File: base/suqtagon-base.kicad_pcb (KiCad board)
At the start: 2 copper layers, 100 x 86.6 mm, 13 parts

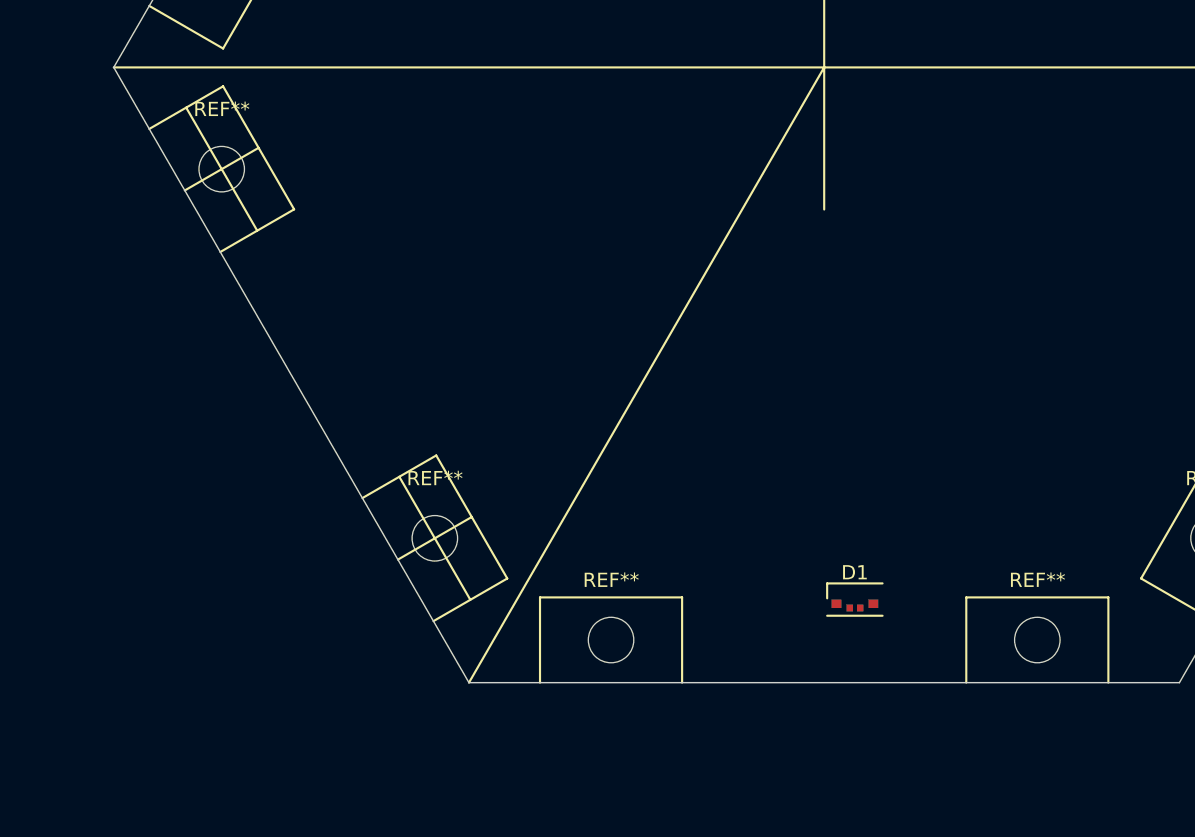
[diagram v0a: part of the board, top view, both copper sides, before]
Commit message: side single gerber
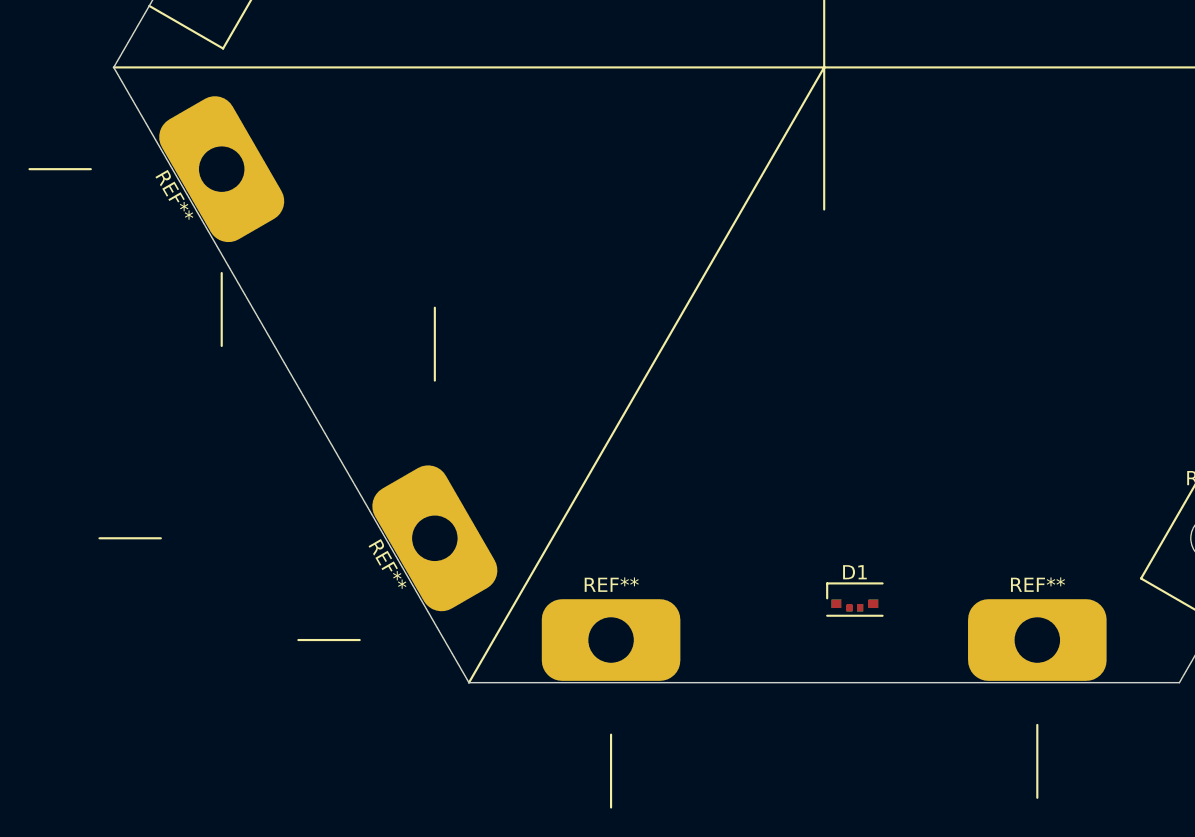
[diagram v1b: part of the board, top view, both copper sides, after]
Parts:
- removed the REF** at (57.6, 100.5)
- removed the REF** at (72.6, 126.4)
- removed the REF** at (85.0, 133.6)
- removed the REF** at (115.0, 133.6)
- added REF**: MountingHole_3.2mm_M3_ISO7380_Pad, MountingHoleConnector:MountingHole_3.2mm_M3_6mmx10mm_Pad, F.Cu at (115.0, 133.6)
- added REF**: MountingHole_3.2mm_M3_ISO7380_Pad, MountingHoleConnector:MountingHole_3.2mm_M3_6mmx10mm_Pad, F.Cu at (72.6, 126.4)
- added REF**: MountingHole_3.2mm_M3_ISO7380_Pad, MountingHoleConnector:MountingHole_3.2mm_M3_6mmx10mm_Pad, F.Cu at (57.6, 100.5)
- added REF**: MountingHole_3.2mm_M3_ISO7380_Pad, MountingHoleConnector:MountingHole_3.2mm_M3_6mmx10mm_Pad, F.Cu at (85.0, 133.6)

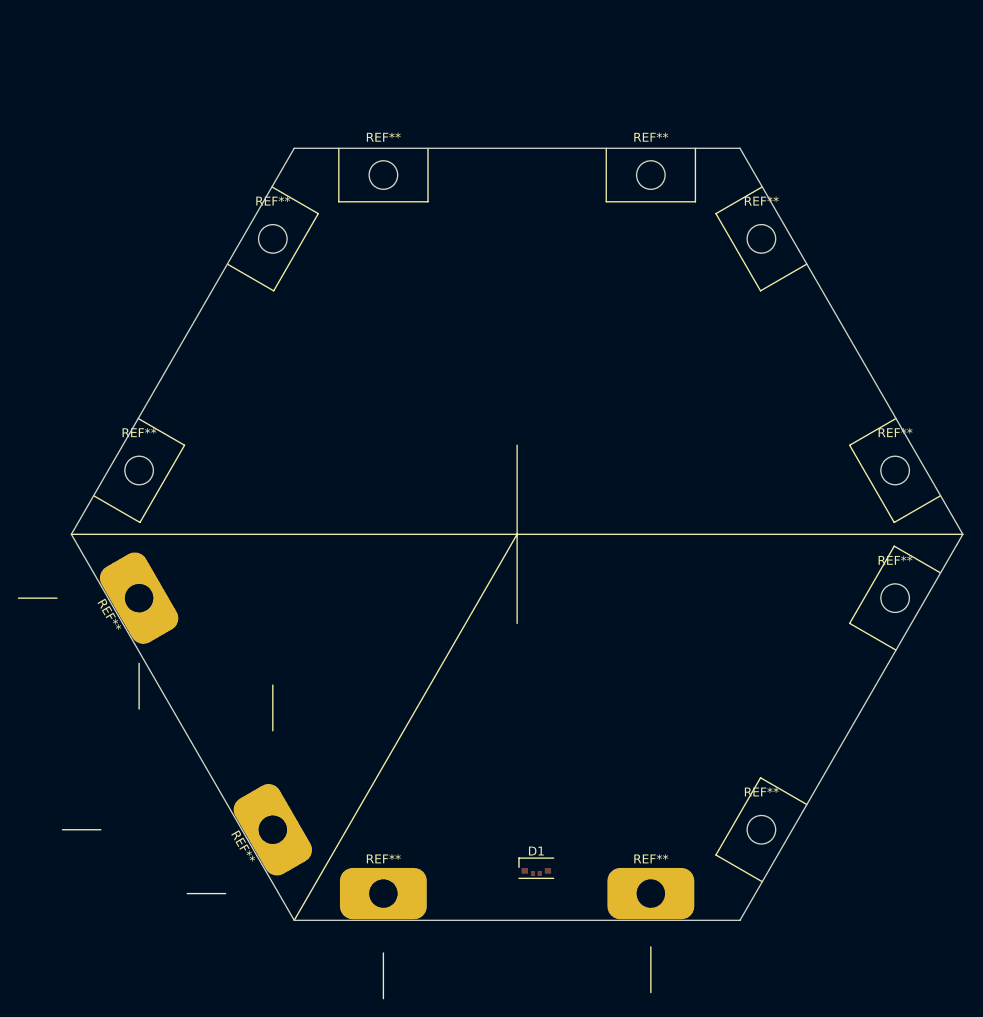
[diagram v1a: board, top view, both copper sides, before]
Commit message: populating some components in base
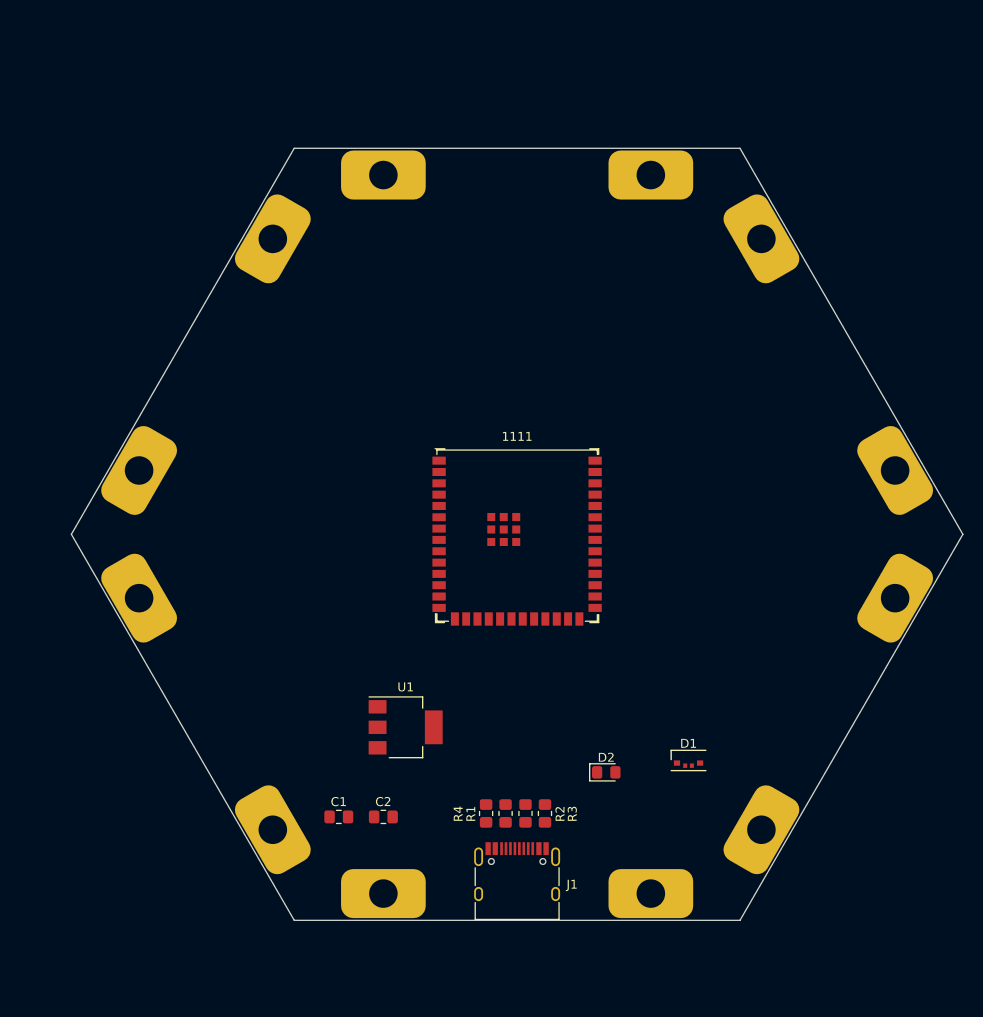
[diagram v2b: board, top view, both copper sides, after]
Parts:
- removed the REF** at (115.0, 53.0)
- removed the REF** at (85.0, 53.0)
- removed the REF** at (142.4, 100.5)
- removed the REF** at (127.4, 126.4)
- removed the REF** at (57.6, 86.1)
- removed the REF** at (127.4, 60.2)
- removed the REF** at (72.6, 60.2)
- removed the REF** at (142.4, 86.1)
- added 1111: ESP32-S3-WROOM-1, Espressif:ESP32-S3-WROOM-1U, F.Cu at (100.0, 93.3)
- added C1: C, Capacitor_SMD:C_0805_2012Metric_Pad1.18x1.45mm_HandSolder, F.Cu at (80.0, 125.0)
- added C2: C, Capacitor_SMD:C_0805_2012Metric_Pad1.18x1.45mm_HandSolder, F.Cu at (85.0, 125.0)
- added D2: D_Schottky, Diode_SMD:D_0805_2012Metric_Pad1.15x1.40mm_HandSolder, F.Cu at (110.0, 120.0)
- added J1: USB_C_Receptacle_USB2.0, Connector_USB:USB_C_Receptacle_HRO_TYPE-C-31-M-12, F.Cu at (100.0, 132.6)
- added R1: 0, Resistor_SMD:R_0805_2012Metric_Pad1.20x1.40mm_HandSolder, F.Cu at (98.7, 124.6)
- added R2: 0, Resistor_SMD:R_0805_2012Metric_Pad1.20x1.40mm_HandSolder, F.Cu at (100.9, 124.6)
- added R3: 5.1k, Resistor_SMD:R_0805_2012Metric_Pad1.20x1.40mm_HandSolder, F.Cu at (103.1, 124.6)
- added R4: 5.1k, Resistor_SMD:R_0805_2012Metric_Pad1.20x1.40mm_HandSolder, F.Cu at (96.5, 124.6)
- added REF**: MountingHole_3.2mm_M3_ISO7380_Pad, MountingHoleConnector:MountingHole_3.2mm_M3_6mmx10mm_Pad, F.Cu at (57.6, 86.1)
- added REF**: MountingHole_3.2mm_M3_ISO7380_Pad, MountingHoleConnector:MountingHole_3.2mm_M3_6mmx10mm_Pad, F.Cu at (72.6, 60.2)
- added REF**: MountingHole_3.2mm_M3_ISO7380_Pad, MountingHoleConnector:MountingHole_3.2mm_M3_6mmx10mm_Pad, F.Cu at (127.4, 126.4)
- added REF**: MountingHole_3.2mm_M3_ISO7380_Pad, MountingHoleConnector:MountingHole_3.2mm_M3_6mmx10mm_Pad, F.Cu at (85.0, 53.0)
- added REF**: MountingHole_3.2mm_M3_ISO7380_Pad, MountingHoleConnector:MountingHole_3.2mm_M3_6mmx10mm_Pad, F.Cu at (115.0, 53.0)
- added REF**: MountingHole_3.2mm_M3_ISO7380_Pad, MountingHoleConnector:MountingHole_3.2mm_M3_6mmx10mm_Pad, F.Cu at (142.4, 86.1)
- added REF**: MountingHole_3.2mm_M3_ISO7380_Pad, MountingHoleConnector:MountingHole_3.2mm_M3_6mmx10mm_Pad, F.Cu at (127.4, 60.2)
- added REF**: MountingHole_3.2mm_M3_ISO7380_Pad, MountingHoleConnector:MountingHole_3.2mm_M3_6mmx10mm_Pad, F.Cu at (142.4, 100.5)
- added U1: AMS1117-3.3, Package_TO_SOT_SMD:SOT-223-3_TabPin2, F.Cu at (87.5, 115.0)
- moved D1 20.9 mm to (119.2, 119.1)

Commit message: added more esp components
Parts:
- added C3: 100uF, Capacitor_SMD:C_0805_2012Metric_Pad1.18x1.45mm_HandSolder, F.Cu at (88.4, 85.0)
- added J2: Conn_01x04_Male, Connector_PinHeader_2.54mm:PinHeader_2x02_P2.54mm_Vertical_SMD, F.Cu at (91.5, 59.5)
- added J3: Conn_01x04_Male, Connector_PinHeader_2.54mm:PinHeader_2x02_P2.54mm_Vertical_SMD, F.Cu at (108.5, 59.5)
- added R5: 100, Resistor_SMD:R_0805_2012Metric_Pad1.20x1.40mm_HandSolder, F.Cu at (80.0, 86.5)
- added R6: 100, Resistor_SMD:R_0805_2012Metric_Pad1.20x1.40mm_HandSolder, F.Cu at (125.0, 116.5)
- added SW1: SW_Push, Button_Switch_SMD:SW_Push_1P1T_NO_6x6mm_H9.5mm, F.Cu at (80.0, 80.0)
- added SW2: SW_Push, Button_Switch_SMD:SW_Push_1P1T_NO_6x6mm_H9.5mm, F.Cu at (125.0, 110.0)
- C1, C2: value C -> 22uF
- moved D1 43.8 mm to (112.9, 75.8)
- moved D2 25.0 mm to (85.0, 120.0)
- moved C2 12.7 mm to (80.8, 113.0), turned to 90 degrees
- moved C1 8.04 mm to (80.8, 117.0), turned to 90 degrees
- renumbered 1111 to 1111111
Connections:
- 1111111 pad 27: unconnected-(1111-Pad27) -> Net-(SW2-Pad1)
- 1111111 pad 3: unconnected-(1111-Pad3) -> Net-(SW1-Pad2)

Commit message: rotated screw blocks to allow flat screws
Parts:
- moved J2 22.6 mm to (80.0, 40.0)
- moved J3 19.8 mm to (111.8, 40.0)
- moved REF** 2.00 mm to (85.0, 55.0), turned to 90 degrees
- moved REF** 2.00 mm to (115.0, 55.0), turned to -90 degrees
- moved REF** 2.00 mm to (85.0, 131.6), turned to -90 degrees
- moved REF** 2.00 mm to (115.0, 131.6), turned to -90 degrees
- moved REF** 2.00 mm to (74.3, 125.4), turned to -150 degrees
- moved REF** 2.00 mm to (59.3, 87.1), turned to 150 degrees
- moved REF** 2.00 mm to (74.3, 61.2), turned to 150 degrees
- moved REF** 2.00 mm to (125.7, 125.4), turned to 150 degrees
- moved REF** 2.00 mm to (140.7, 87.1), turned to -150 degrees
- moved REF** 2.00 mm to (59.3, 99.5), turned to -150 degrees
- moved REF** 2.00 mm to (125.7, 61.2), turned to -150 degrees
- moved REF** 2.00 mm to (140.7, 99.5), turned to 150 degrees

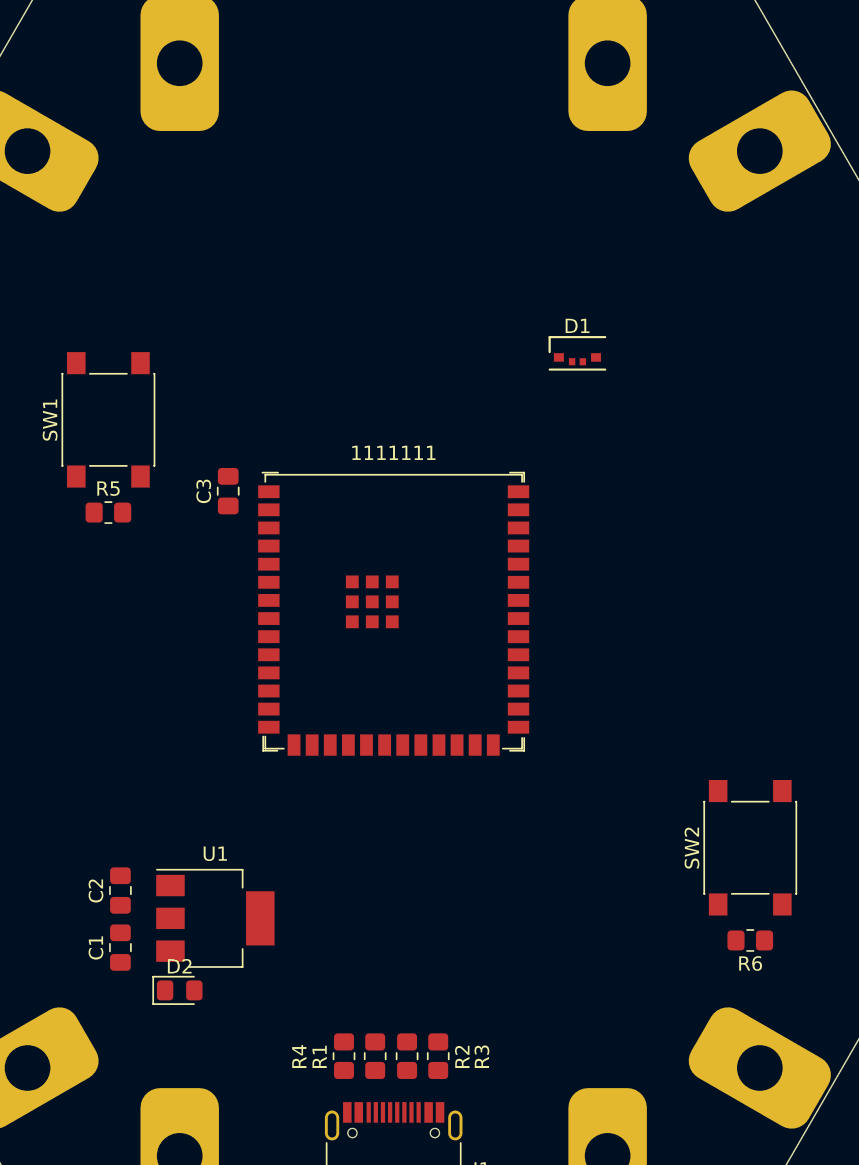
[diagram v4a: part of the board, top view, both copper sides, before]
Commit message: started reverse led with pcb cut
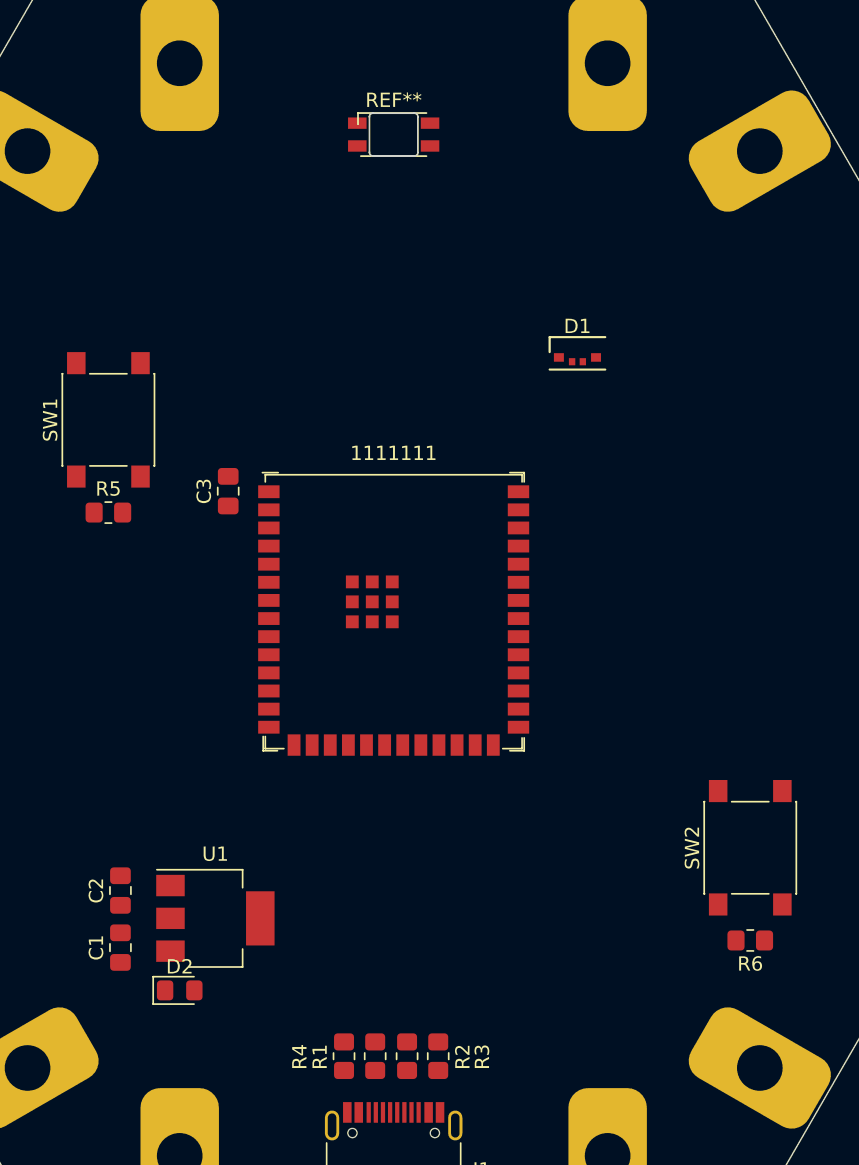
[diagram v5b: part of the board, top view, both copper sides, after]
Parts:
- added REF**: LED_RGB_SMD_6028_2.8x3.5mm_Square, LED_SMD_REVERSE_MOUNT:LED_RGB_SMD_6028_2.8x3.5mm_Square, F.Cu at (100.0, 60.0)
